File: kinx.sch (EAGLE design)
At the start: 45 parts, among them T1 MCP1825S

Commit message: fix MPN/OC_MOUSER for the molex 105133-0011 connectors
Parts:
- USBFS, USBHS: MP (none) -> 105133-0011; OC_MOUSER 538-105133-0001 -> 538-105133-0011
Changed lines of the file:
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@@
 <grid distance="0.1" unitdist="inch" unit="inch" style="lines" multiple="1" display="no" altdistance="0.01" altunitdist="inch" altunit="inch"/>
 <layers>
-<layer number="1" name="Top" color="4" fill="1" visible="yes" active="no"/>
-<layer number="2" name="Route2" color="10" fill="1" visible="yes" active="no"/>
-<layer number="3" name="Route3" color="4" fill="3" visible="yes" active="no"/>
-<layer number="4" name="Route4" color="1" fill="4" visible="yes" active="no"/>
-<layer number="5" name="Route5" color="4" fill="4" visible="yes" active="no"/>
-<layer number="6" name="Route6" color="1" fill="8" visible="yes" active="no"/>
-<layer number="7" name="Route7" color="4" fill="8" visible="yes" active="no"/>
-<layer number="8" name="Route8" color="1" fill="2" visible="yes" active="no"/>
-<layer number="9" name="Route9" color="4" fill="2" visible="yes" active="no"/>
-<layer number="10" name="Route10" color="1" fill="7" visible="yes" active="no"/>
-<layer number="11" name="Route11" color="4" fill="7" visible="yes" active="no"/>
-<layer number="12" name="Route12" color="1" fill="5" visible="yes" active="no"/>
-<layer number="13" name="Route13" color="4" fill="5" visible="yes" active="no"/>
-<layer number="14" name="Route14" color="1" fill="6" visible="yes" active="no"/>
-<layer number="15" name="Route15" color="14" fill="1" visible="yes" active="no"/>
-<layer number="16" name="Bottom" color="1" fill="1" visible="yes" active="no"/>
-<layer number="17" name="Pads" color="2" fill="1" visible="yes" active="no"/>
-<layer number="18" name="Vias" color="2" fill="1" visible="yes" active="no"/>
-<layer number="19" name="Unrouted" color="6" fill="1" visible="yes" active="no"/>
-<layer number="20" name="Dimension" color="15" fill="1" visible="yes" active="no"/>
-<layer number="21" name="tPlace" color="7" fill="1" visible="yes" active="no"/>
-<layer number="22" name="bPlace" color="7" fill="1" visible="yes" active="no"/>
-<layer number="23" name="tOrigins" color="15" fill="1" visible="yes" active="no"/>
-<layer number="24" name="bOrigins" color="15" fill="1" visible="yes" active="no"/>
-<layer number="25" name="tNames" color="7" fill="1" visible="yes" active="no"/>
-<layer number="26" name="bNames" color="7" fill="1" visible="yes" active="no"/>
-<layer number="27" name="tValues" color="7" fill="1" visible="yes" active="no"/>
-<layer number="28" name="bValues" color="7" fill="1" visible="yes" active="no"/>
+<layer number="1" name="Top" color="4" fill="1" visible="no" active="no"/>
+<layer number="2" name="Route2" color="10" fill="1" visible="no" active="no"/>
+<layer number="3" name="Route3" color="4" fill="3" visible="no" active="no"/>
+<layer number="4" name="Route4" color="1" fill="4" visible="no" active="no"/>
+<layer number="5" name="Route5" color="4" fill="4" visible="no" active="no"/>
+<layer number="6" name="Route6" color="1" fill="8" visible="no" active="no"/>
+<layer number="7" name="Route7" color="4" fill="8" visible="no" active="no"/>
+<layer number="8" name="Route8" color="1" fill="2" visible="no" active="no"/>
+<layer number="9" name="Route9" color="4" fill="2" visible="no" active="no"/>
+<layer number="10" name="Route10" color="1" fill="7" visible="no" active="no"/>
+<layer number="11" name="Route11" color="4" fill="7" visible="no" active="no"/>
+<layer number="12" name="Route12" color="1" fill="5" visible="no" active="no"/>
+<layer number="13" name="Route13" color="4" fill="5" visible="no" active="no"/>
+<layer number="14" name="Route14" color="1" fill="6" visible="no" active="no"/>
+<layer number="15" name="Route15" color="14" fill="1" visible="no" active="no"/>
+<layer number="16" name="Bottom" color="1" fill="1" visible="no" active="no"/>
+<layer number="17" name="Pads" color="2" fill="1" visible="no" active="no"/>
+<layer number="18" name="Vias" color="2" fill="1" visible="no" active="no"/>
+<layer number="19" name="Unrouted" color="6" fill="1" visible="no" active="no"/>
+<layer number="20" name="Dimension" color="15" fill="1" visible="no" active="no"/>
+<layer number="21" name="tPlace" color="7" fill="1" visible="no" active="no"/>
+<layer number="22" name="bPlace" color="7" fill="1" visible="no" active="no"/>
+<layer number="23" name="tOrigins" color="15" fill="1" visible="no" active="no"/>
+<layer number="24" name="bOrigins" color="15" fill="1" visible="no" active="no"/>
+<layer number="25" name="tNames" color="7" fill="1" visible="no" active="no"/>
+<layer number="26" name="bNames" color="7" fill="1" visible="no" active="no"/>
+<layer number="27" name="tValues" color="7" fill="1" visible="no" active="no"/>
+<layer number="28" name="bValues" color="7" fill="1" visible="no" active="no"/>
 <layer number="29" name="tStop" color="7" fill="3" visible="no" active="no"/>
 <layer number="30" name="bStop" color="7" fill="6" visible="no" active="no"/>
@@
 <layer number="35" name="tGlue" color="7" fill="4" visible="no" active="no"/>
 <layer number="36" name="bGlue" color="7" fill="5" visible="no" active="no"/>
-<layer number="37" name="tTest" color="7" fill="1" visible="yes" active="no"/>
-<layer number="38" name="bTest" color="7" fill="1" visible="yes" active="no"/>
+<layer number="37" name="tTest" color="7" fill="1" visible="no" active="no"/>
+<layer number="38" name="bTest" color="7" fill="1" visible="no" active="no"/>
 <layer number="39" name="tKeepout" color="4" fill="11" visible="no" active="no"/>
 <layer number="40" name="bKeepout" color="1" fill="11" visible="no" active="no"/>
@@
 <layer number="44" name="Drills" color="7" fill="1" visible="no" active="no"/>
 <layer number="45" name="Holes" color="7" fill="1" visible="no" active="no"/>
-<layer number="46" name="Milling" color="3" fill="1" visible="yes" active="no"/>
-<layer number="47" name="Measures" color="7" fill="1" visible="yes" active="no"/>
-<layer number="48" name="Document" color="7" fill="1" visible="yes" active="no"/>
-<layer number="49" name="Reference" color="7" fill="1" visible="yes" active="no"/>
-<layer number="50" name="dxf" color="7" fill="1" visible="yes" active="no"/>
-<layer number="51" name="tDocu" color="7" fill="1" visible="yes" active="no"/>
-<layer number="52" name="bDocu" color="7" fill="1" visible="yes" active="no"/>
-<layer number="53" name="tGND_GNDA" color="7" fill="1" visible="yes" active="no"/>
-<layer number="54" name="bGND_GNDA" color="7" fill="1" visible="yes" active="no"/>
-<layer number="56" name="wert" color="7" fill="1" visible="yes" active="no"/>
-<layer number="57" name="tCAD" color="7" fill="1" visible="yes" active="no"/>
-<layer number="59" name="tCarbon" color="7" fill="1" visible="yes" active="no"/>
-<layer number="60" name="bCarbon" color="7" fill="1" visible="yes" active="no"/>
+<layer number="46" name="Milling" color="3" fill="1" visible="no" active="no"/>
+<layer number="47" name="Measures" color="7" fill="1" visible="no" active="no"/>
+<layer number="48" name="Document" color="7" fill="1" visible="no" active="no"/>
+<layer number="49" name="Reference" color="7" fill="1" visible="no" active="no"/>
+<layer number="50" name="dxf" color="7" fill="1" visible="no" active="no"/>
+<layer number="51" name="tDocu" color="7" fill="1" visible="no" active="no"/>
+<layer number="52" name="bDocu" color="7" fill="1" visible="no" active="no"/>
+<layer number="53" name="tGND_GNDA" color="7" fill="1" visible="no" active="no"/>
+<layer number="54" name="bGND_GNDA" color="7" fill="1" visible="no" active="no"/>
+<layer number="56" name="wert" color="7" fill="1" visible="no" active="no"/>
+<layer number="57" name="tCAD" color="7" fill="1" visible="no" active="no"/>
+<layer number="59" name="tCarbon" color="7" fill="1" visible="no" active="no"/>
+<layer number="60" name="bCarbon" color="7" fill="1" visible="no" active="no"/>
 <layer number="88" name="SimResults" color="9" fill="1" visible="yes" active="yes"/>
 <layer number="89" name="SimProbes" color="9" fill="1" visible="yes" active="yes"/>
@@
 <part name="USBFS" library="molex-105133-0001" deviceset="105133-0001" device="">
 <attribute name="DIGIKEY" value="WM10134CT-ND"/>
-<attribute name="OC_MOUSER" value="538-105133-0001"/>
+<attribute name="MP" value="105133-0011"/>
+<attribute name="OC_MOUSER" value="538-105133-0011"/>
 </part>
 <part name="USBHS" library="molex-105133-0001" deviceset="105133-0001" device="">
 <attribute name="DIGIKEY" value="WM10134CT-ND"/>
-<attribute name="OC_MOUSER" value="538-105133-0001"/>
+<attribute name="MP" value="105133-0011"/>
+<attribute name="OC_MOUSER" value="538-105133-0011"/>
 </part>
 <part name="+3V1" library="supply1" library_urn="urn:adsk.eagle:library:371" deviceset="+3V3" device=""/>

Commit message: Clean up schematic (no board changes)
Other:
- note added: "USB"
- note added: "columns"
- note added: "left keywell"
- note added: "left thumb pad"
- note added: "not connected"
- note added: "power supply"
- note added: "right keywell"
- note added: "right thumb pad"
- note added: "top"

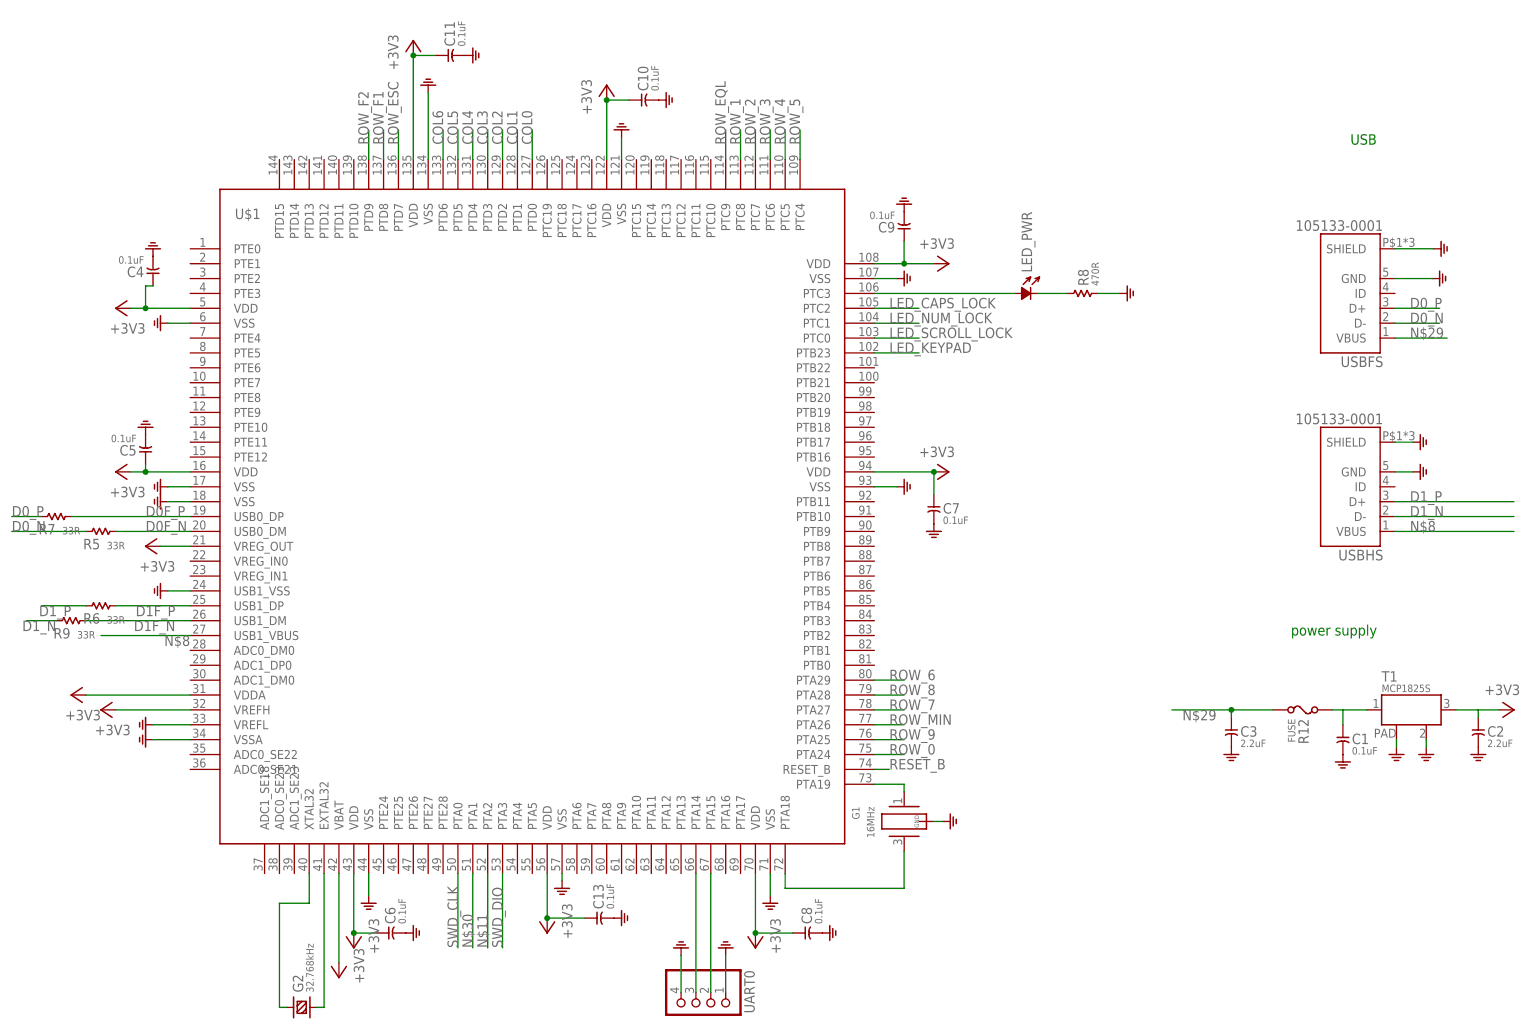
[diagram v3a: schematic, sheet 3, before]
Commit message: better net names
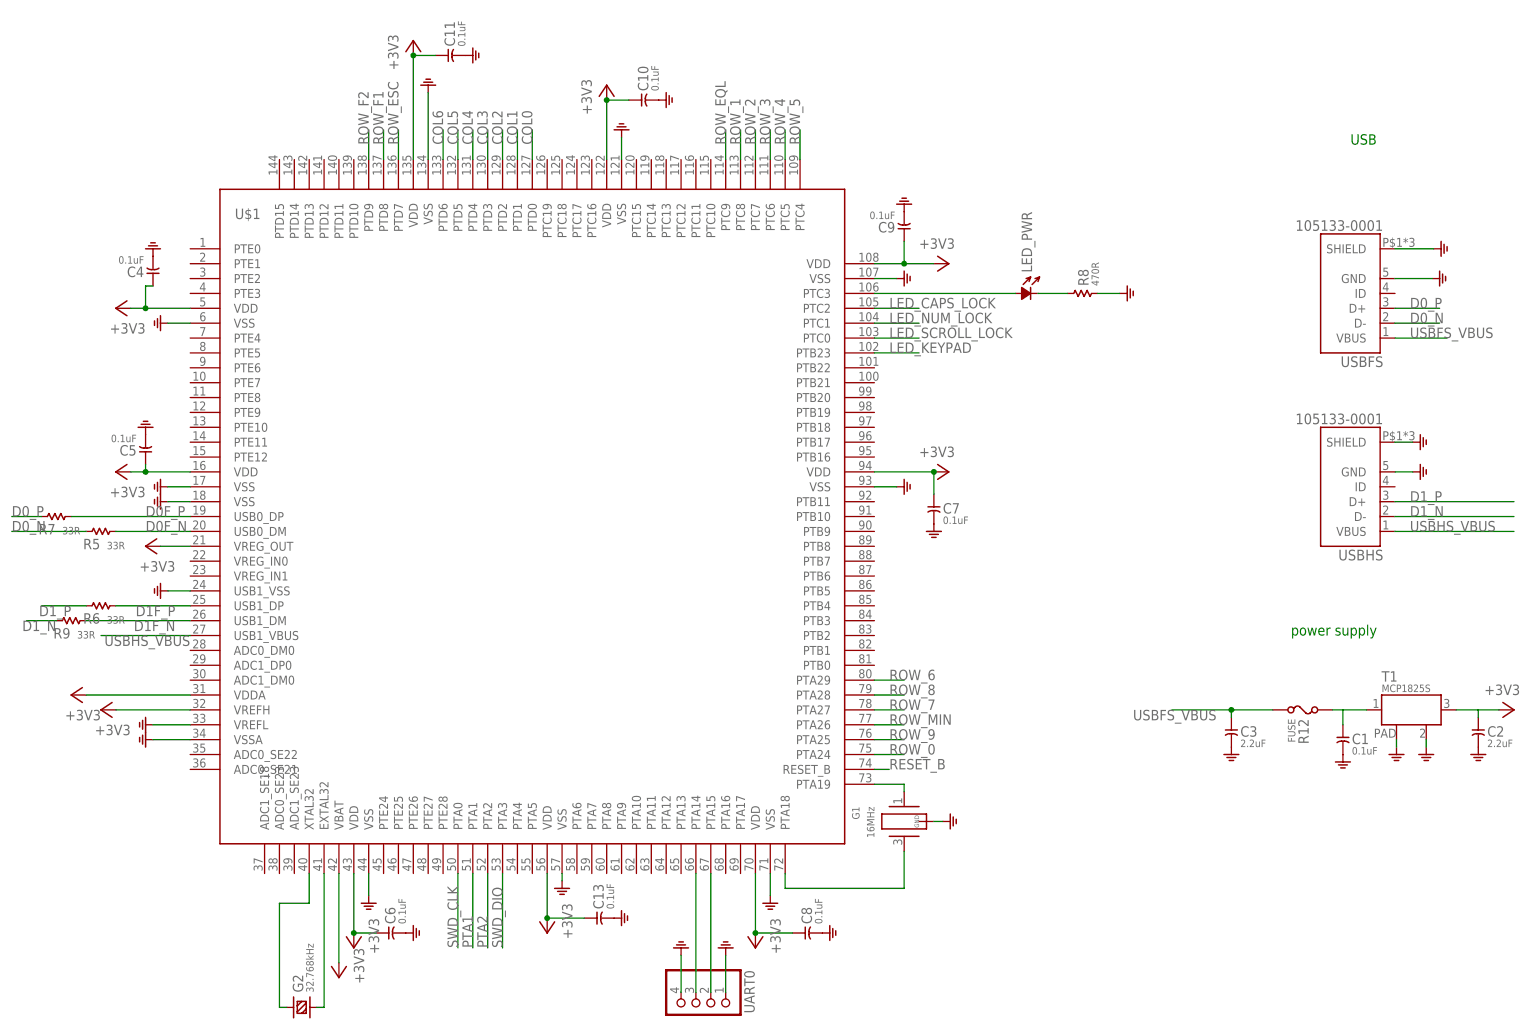
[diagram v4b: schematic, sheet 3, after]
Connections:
- net N$11 renamed PTA2
- net N$29 renamed USBFS_VBUS
- net N$30 renamed PTA1
- net N$8 renamed USBHS_VBUS
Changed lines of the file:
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@@
 </segment>
 </net>
-<net name="N$29" class="2">
+<net name="USBFS_VBUS" class="2">
 <segment>
 <pinref part="C3" gate="G$1" pin="1"/>
@@
 </segment>
 </net>
-<net name="N$30" class="0">
+<net name="PTA1" class="0">
 <segment>
 <pinref part="U$1" gate="G$1" pin="PTA1"/>
@@
 </segment>
 </net>
-<net name="N$11" class="0">
+<net name="PTA2" class="0">
 <segment>
 <pinref part="U$1" gate="G$1" pin="PTA2"/>
@@
 </segment>
 </net>
-<net name="N$8" class="0">
+<net name="USBHS_VBUS" class="0">
 <segment>
 <pinref part="U$1" gate="G$1" pin="USB1_VBUS"/>
@@
 </segment>
 </net>
-<net name="N$30" class="0">
+<net name="PTA1" class="0">
 <segment>
 <pinref part="MKL04Z32VLC4" gate="G$1" pin="PTA6"/>
@@
 </segment>
 </net>
-<net name="N$11" class="0">
+<net name="PTA2" class="0">
 <segment>
 <pinref part="MKL04Z32VLC4" gate="G$1" pin="PTB1"/>
